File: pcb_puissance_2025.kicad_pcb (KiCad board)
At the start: 4 copper layers, 150 x 90 mm, 143 parts, among them J1 1755736, J10 1755736, J11 USB_C_Receptacle_USB2.0_16P, J12 1755736, J13 1755736, J14 Conn_02x06_Odd_Even, J15 1755736, J16 1755736, J17 Conn_02x06_Odd_Even, J18 1755736, J19 1755736, J2 1755736, J20 Conn_02x06_Odd_Even, J21 1755736, J22 1755736, J3 1755736, J4 1755736, J5 1755736, J6 1755736, J7 Conn_02x10_Odd_Even, J8 Conn_ST_STDC14, Q1 SUD50P06-15, Q2 SUD50P06-15, Q3 SUD50P06-15, Q4 SUD50P06-15, Q5 SUD50P06-15, Q6 SUD50P06-15, Q7 STL40DN3LLH5, Q8 NPN, Q9 NMOS, SW1 SW_Push, U1 LTC4417IGN, U10 MCP9808T-E/MS, U2 STM32G491KEU6, U3 INA236BIDDFR, U4 INA236AIDDFR, U5 INA236AIDDFR, U6 INA236AIDDFR, U7 INA236BIDDFR, U8 INA236BIDDFR, U9 TCPP02-M18

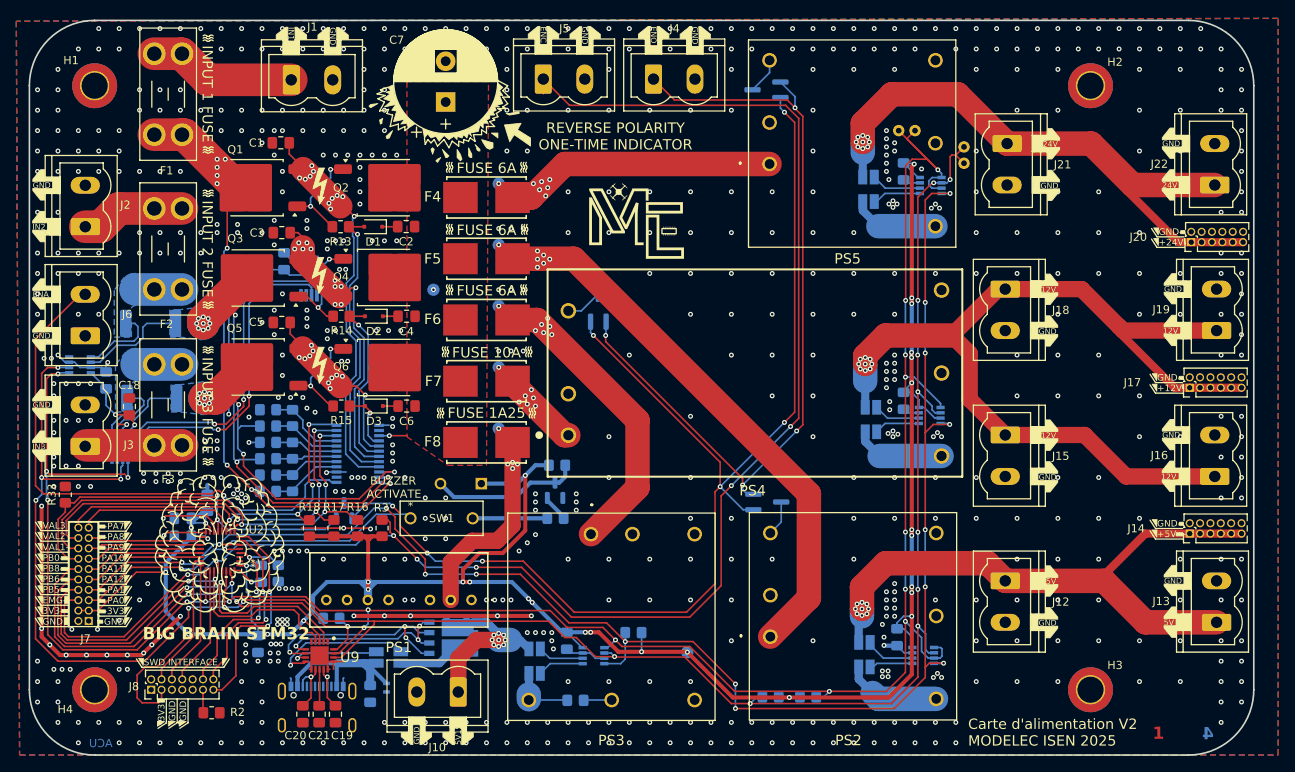
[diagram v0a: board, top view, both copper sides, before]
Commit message: Correctifs et améliorations + passage à KiCad V9
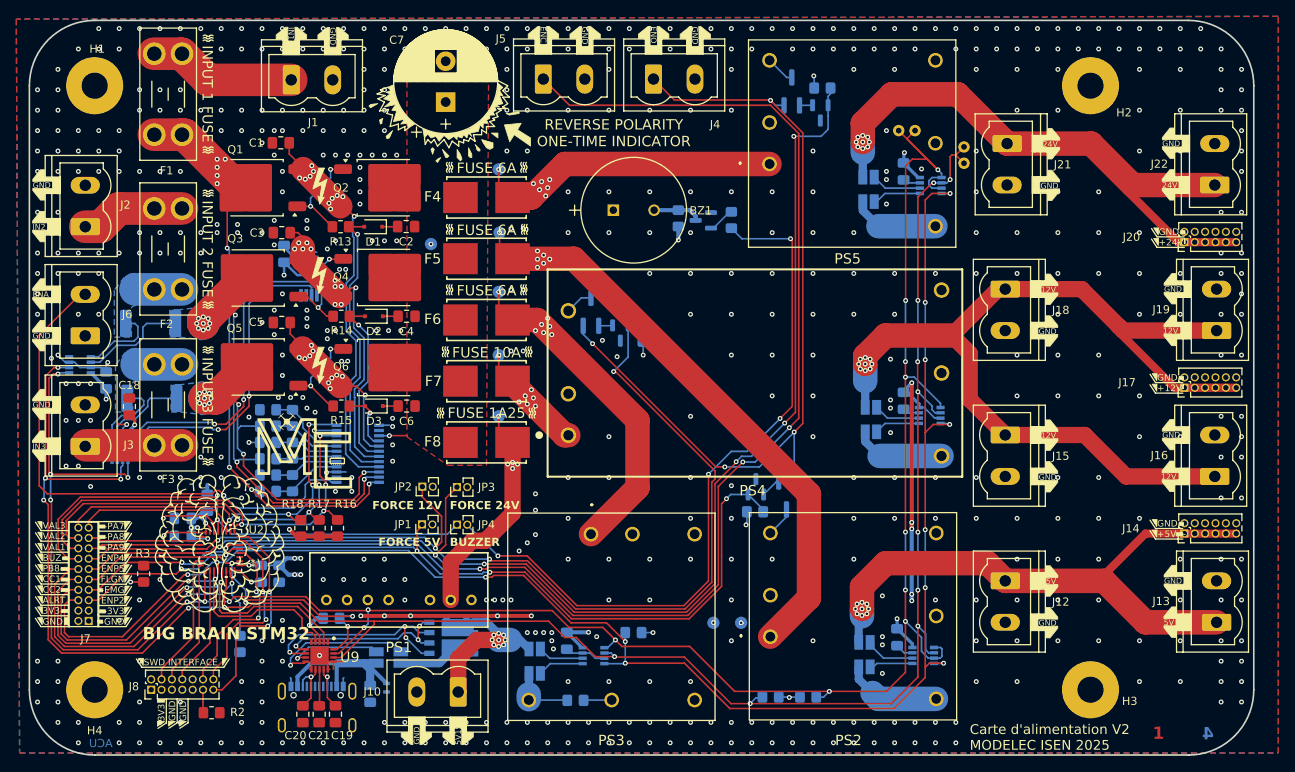
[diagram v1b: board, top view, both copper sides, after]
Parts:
- removed SW1: SW_Push, Modelec:SW_DS01-254-L-01BE_CUD
- added JP1: Jumper_2_Open, Connector_PinHeader_1.27mm:PinHeader_1x02_P1.27mm_Vertical, F.Cu at (157.1, 120.8)
- added JP2: Jumper_2_Open, Connector_PinHeader_1.27mm:PinHeader_1x02_P1.27mm_Vertical, F.Cu at (157.1, 116.1)
- added JP3: Jumper_2_Open, Connector_PinHeader_1.27mm:PinHeader_1x02_P1.27mm_Vertical, F.Cu at (161.4, 116.2)
- added JP4: Jumper_2_Bridged, Connector_PinHeader_1.27mm:PinHeader_1x02_P1.27mm_Vertical, F.Cu at (161.4, 120.8)
- added Q10: NMOS, Package_TO_SOT_SMD:SOT-23, B.Cu at (181.4, 97.3)
- added Q11: NMOS, Package_TO_SOT_SMD:SOT-23, B.Cu at (198.0, 116.1)
- added R34: 1k, Resistor_SMD:R_0805_2012Metric_Pad1.20x1.40mm_HandSolder, B.Cu at (184.2, 97.4)
- added R35: 1k, Resistor_SMD:R_0805_2012Metric_Pad1.20x1.40mm_HandSolder, B.Cu at (197.9, 119.2)
- BZ1: moved to F.Cu
- C1, C3, C5: value 0u4 -> 0u39
- C19, C20: value 330u -> 330p
- C2, C4, C6: value 40n -> 39n
- H1, H2, H3, H4: footprint MountingHole:MountingHole_3.2mm_M3_ISO14580_Pad_TopBottom -> MountingHole:MountingHole_3.2mm_M3_Pad
- R13, R14, R15: value 8k06 -> 11k5
- R32: value 1k -> 10k
- R33: moved to B.Cu
- moved R33 105.3 mm to (206.2, 67.3), turned to 180 degrees
- moved Q9 76.0 mm to (205.9, 70.3), turned to -90 degrees
- moved REF** 54.9 mm to (229.1, 84.4)
- moved REF** 54.9 mm to (236.1, 82.4)
- moved REF** 54.9 mm to (241.1, 97.2)
- moved REF** 54.9 mm to (228.1, 87.4)
- moved REF** 54.9 mm to (233.1, 81.4)
- moved G*** 49.4 mm to (142.8, 111.8)
- moved R27 42.4 mm to (195.0, 83.5), turned to 90 degrees
- moved Q8 37.7 mm to (191.6, 83.5), turned to 180 degrees
- moved BZ1 37.2 mm to (180.5, 82.2), turned to 0 degrees
- moved TP1 34.1 mm to (196.2, 132.8)
- moved R31 33.7 mm to (188.5, 83.2), turned to 90 degrees
- moved R3 29.7 mm to (123.0, 126.8)
- moved R32 9.84 mm to (134.8, 135.4)
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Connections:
- net /12V renamed /Converters/12V
- net /24V renamed /Converters/24V
- net /5V renamed /Converters/5V
- net /5V15 renamed /Converters/5V15
- net /Microcontroller/PA0 renamed /Converters/5V_PILOT
- net /Microcontroller/PA10 renamed /Converters/12V_PILOT
- net /power_input_selector/VOUT renamed /Converters/VIN
- D5 pad 1: /Microcontroller/PWR_CTRL -> Net-(Q11-S)
- D5 pad 2: Net-(D5-K-Pad2) -> /Converters/EMERGENCY_STOP
- D6 pad 1: Net-(D5-K-Pad2) -> Net-(Q10-S)
- D6 pad 2: /Microcontroller/PWR_CTRL -> /Converters/EMERGENCY_STOP
- D7 pad 1: Net-(D5-K-Pad2) -> Net-(Q9-S)
- D7 pad 2: /Microcontroller/PWR_CTRL -> /Converters/EMERGENCY_STOP
- J4 pad 1: Net-(D5-K-Pad2) -> /Converters/EMERGENCY_STOP
- J5 pad 1: /Microcontroller/EMG_PUSHED -> /Microcontroller/PA1
- J7 pad 11: /Microcontroller/PA11 -> /Converters/24V_PILOT
- J7 pad 12: /Microcontroller/FLGN -> /Microcontroller/PB8
- J7 pad 6: /Microcontroller/EMG_PUSHED -> /Microcontroller/24VALERT
- J7 pad 7: /Microcontroller/24VALERT -> /Microcontroller/PA1
- J7 pad 9: /Microcontroller/PA12 -> /Microcontroller/FLGN
- J8 pad 3: /3V3 -> unconnected-(J8-VCC-Pad3)
- Q9 pad 1: /Microcontroller/PWR_CTRL -> Net-(Q9-S)
- Q9 pad 2: /Microcontroller/PB0 -> /Converters/24V_PILOT
- R3 pad 1: /Microcontroller/EMG_PUSHED -> /Microcontroller/PA1
- R32 pad 2: Net-(J8-~{RST}) -> /Microcontroller/PB8
- R33 pad 1: /Microcontroller/PB0 -> /Converters/24V_PILOT
- R33 pad 2: GND -> /3V3
- U2 pad 21: /Microcontroller/PA11 -> /Converters/24V_PILOT
- U2 pad 22: /Microcontroller/PA12 -> /Microcontroller/FLGN
- U2 pad 28: /Microcontroller/EMG_PUSHED -> /Microcontroller/24VALERT
- U2 pad 31: /Microcontroller/FLGN -> /Microcontroller/PB8
- U2 pad 6: /Microcontroller/24VALERT -> /Microcontroller/PA1
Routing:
- net /3V3: track 477.0 -> 131.2 mm, vias 34 -> 30
- net /Microcontroller/EMG_PUSHED: track 197.4 -> 0.00 mm, vias 7 -> 0
- net /Microcontroller/PA1: track 0.00 -> 181.2 mm, vias 0 -> 5
- net /Converters/24V_PILOT: track 0.00 -> 162.2 mm, vias 0 -> 6
- net /Microcontroller/PWR_CTRL: track 149.4 -> 0.00 mm, vias 7 -> 0
- net /Converters/12V_PILOT: track 14.2 -> 130.7 mm, vias 0 -> 4
- net /Converters/EMERGENCY_STOP: track 0.00 -> 101.5 mm, vias 0 -> 4
- net Net-(D5-K-Pad2): track 101.4 -> 0.00 mm, vias 4 -> 0
- net Net-(JP4-B): track 9.14 -> 90.1 mm, vias 0 -> 4
- net /Converters/5V_PILOT: track 46.0 -> 107.6 mm, vias 2 -> 5
- net GND: track 125.9 -> 79.7 mm, vias 740 -> 617
- net /Microcontroller/PB8: track 0.00 -> 44.0 mm, vias 0 -> 2
- net /Microcontroller/FLGN: track 60.0 -> 44.9 mm
- net /Microcontroller/PA12: track 14.8 -> 0.00 mm
- net /Microcontroller/PA11: track 14.5 -> 0.00 mm
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- added copper zone on In2.Cu, net /3V3
- removed copper zone on In2.Cu, net GND
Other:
- board text added: "--EMG"
- board text added: "ALRT"
- board text added: "BUZ--"
- board text added: "BUZZER"
- board text added: "CC1---"
- board text added: "CC2---"
- board text added: "ENP2"
- board text added: "ENP4"
- board text added: "ENP5"
- board text added: "FLGN"
- board text added: "FORCE 12V"
- board text added: "FORCE 24V"
- board text added: "FORCE 5V"
- board text added: "VAL1"
- board text removed: "---PA0"
- board text removed: "---PA1"
- board text removed: "BUZZER ACTIVATE"
- board text removed: "EMG-"
- board text removed: "PA10"
- board text removed: "PA11"
- board text removed: "PA12"
- board text removed: "PB0---"
- board text removed: "PB5---"
- board text removed: "PB6---"
- board text removed: "VAL1-"
